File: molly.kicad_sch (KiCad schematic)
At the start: 52 parts, among them J1 QWIIC, J2 QWIIC, J3 QWIIC+, J4 QWIIC+, J5 OLED, SW1 Cherry MX, SW10 Cherry MX, SW11 Cherry MX, SW12 Cherry MX, SW13 Cherry MX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

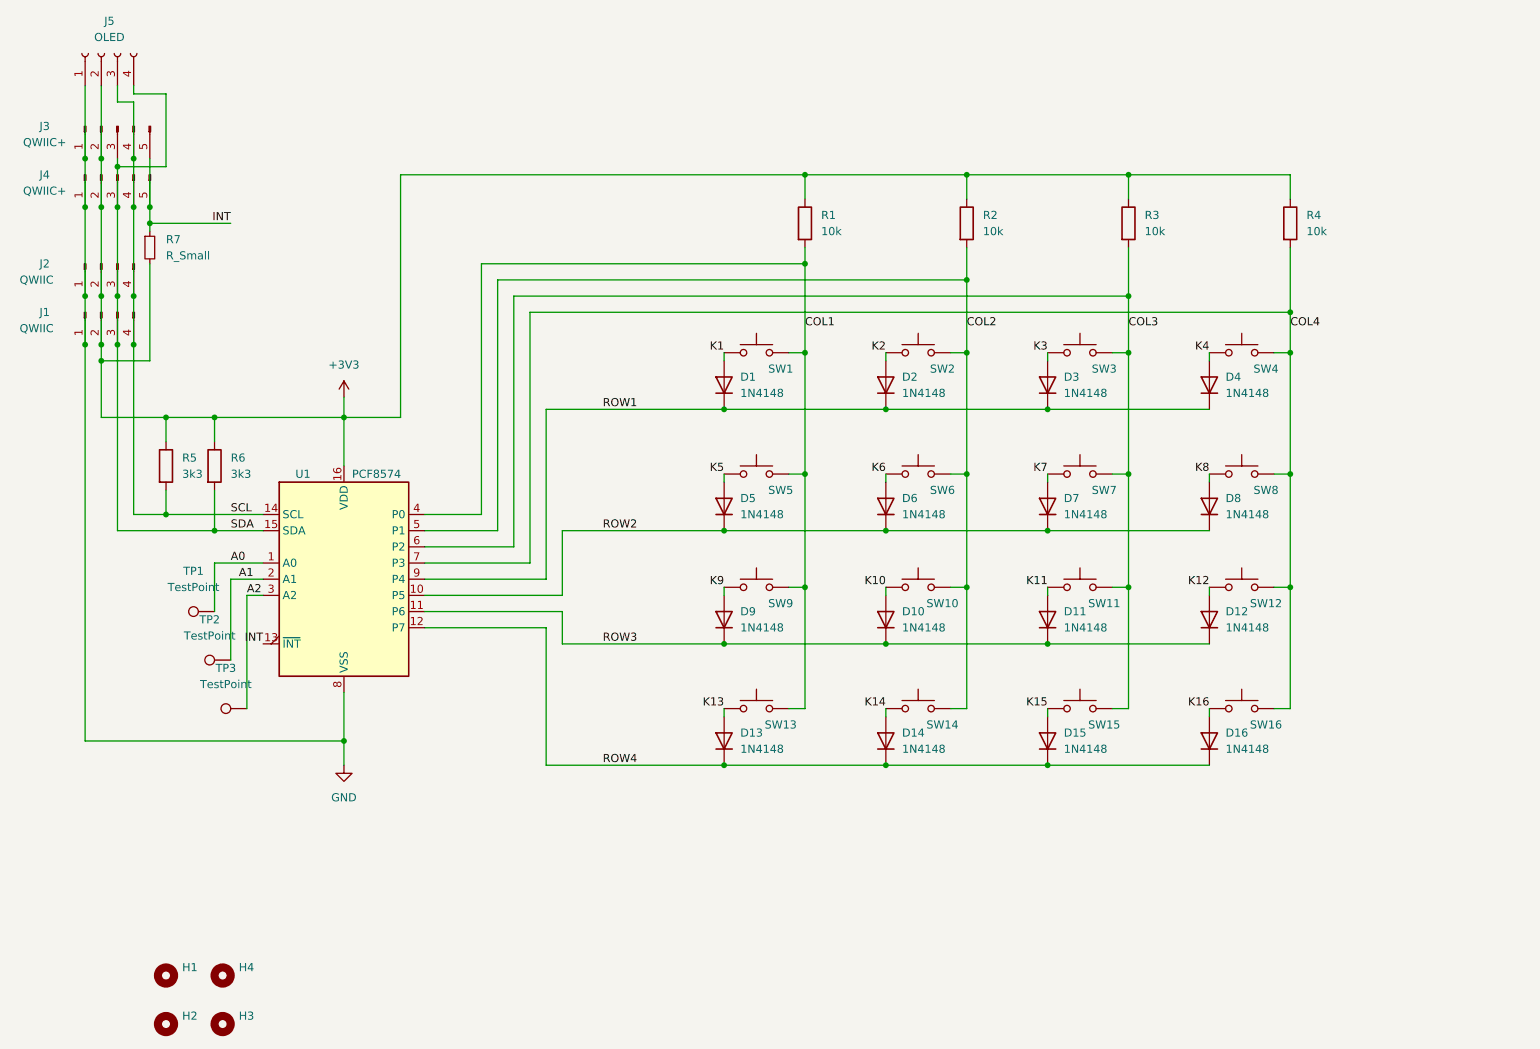
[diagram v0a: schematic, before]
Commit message: Updated for more recent kicads, fix bassackwards screen pinout
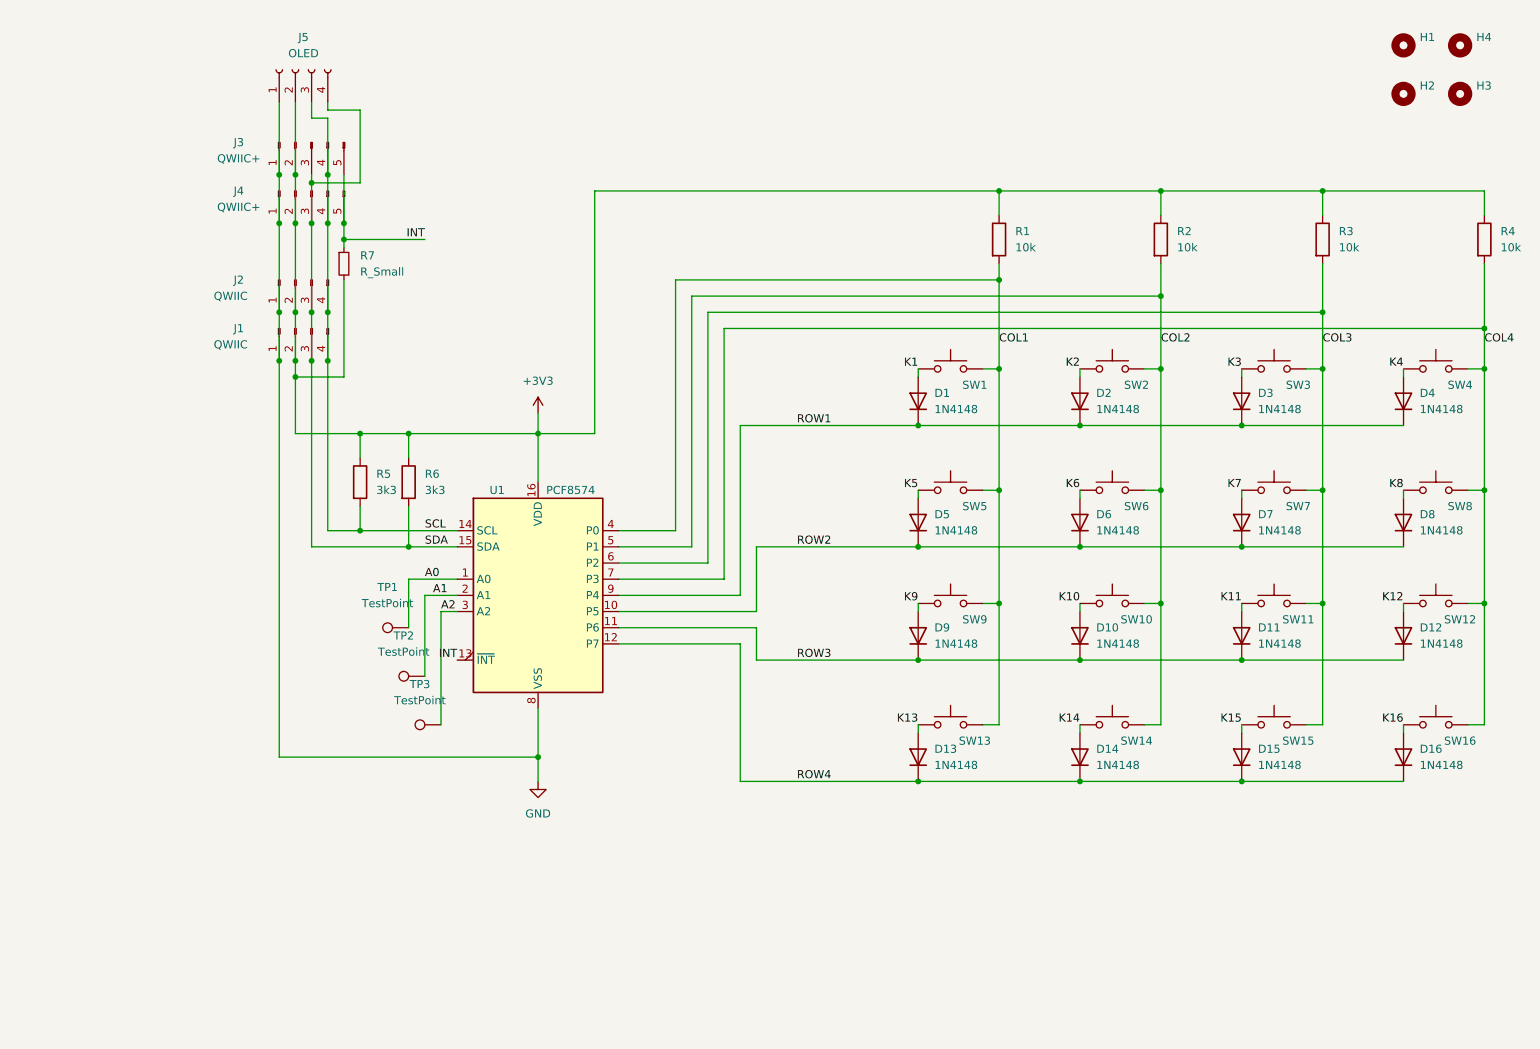
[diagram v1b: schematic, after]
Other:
- moved on the sheet: D1, D10, D11, D12, D13, D14, D15, D16, D2, D3, D4, D5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
